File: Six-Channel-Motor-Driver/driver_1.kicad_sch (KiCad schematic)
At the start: 9 parts, among them J2 Screw_Terminal_01x02, Q1 Q_NMOS_GDS, Q2 Q_NMOS_GDS, Q3 Q_NMOS_GDS, Q4 Q_NMOS_GDS

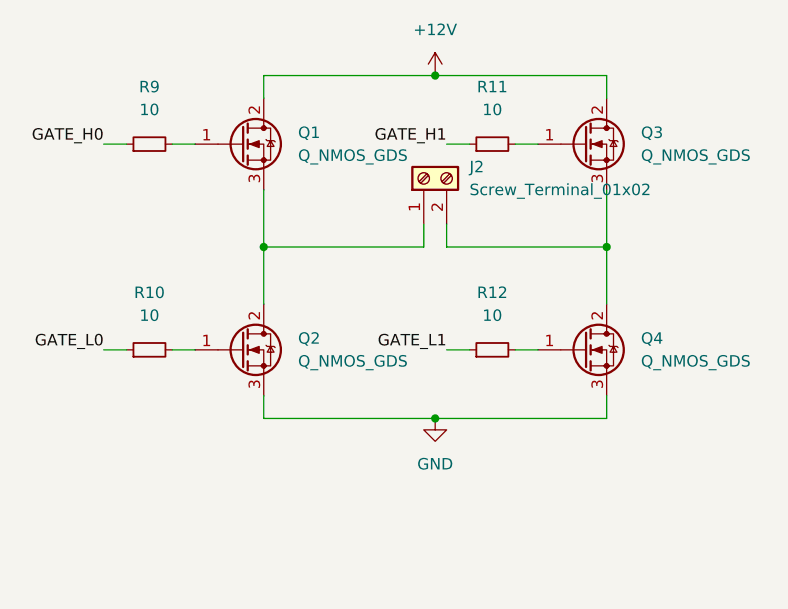
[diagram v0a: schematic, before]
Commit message: Added start of driver blocks
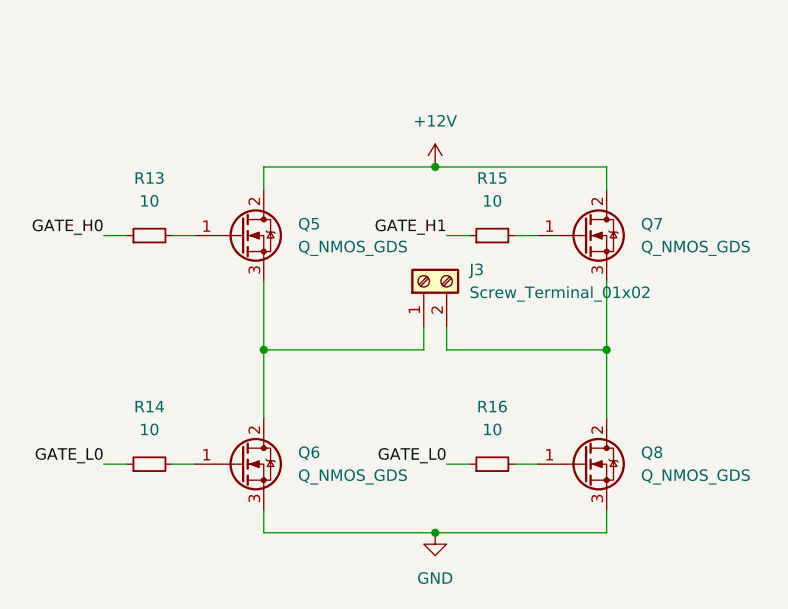
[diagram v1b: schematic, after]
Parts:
- removed J2: Screw_Terminal_01x02, Connector_Wire:SolderWire-2.5sqmm_1x02_P8.8mm_D2.4mm_OD4.4mm, symbol Connector:Screw_Terminal_01x02
- removed Q1, Q2, Q3, Q4: Q_NMOS_GDS, Package_TO_SOT_SMD:SOT-23, symbol Device:Q_NMOS_GDS
- removed R10, R11, R12, R9: 10, Resistor_SMD:R_0603_1608Metric, symbol Device:R_Small
- added J3: Screw_Terminal_01x02, Connector_Wire:SolderWire-2.5sqmm_1x02_P8.8mm_D2.4mm_OD4.4mm, symbol Connector:Screw_Terminal_01x02
- added Q5, Q6, Q7, Q8: Q_NMOS_GDS, Package_TO_SOT_SMD:SOT-23, symbol Device:Q_NMOS_GDS
- added R13, R14, R15, R16: 10, Resistor_SMD:R_0603_1608Metric, symbol Device:R_Small
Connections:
- net +12V: now also Q5.2 (D), Q7.2 (D)
- net GATE_H0: now also R13.1
- net GATE_H1: now also R15.1
- net GATE_L0: now also R14.1, R16.1
- net GND: now also Q6.3 (S), Q8.3 (S)
- new net: Q6.1 (G), R14.2
- new net: Q7.1 (G), R15.2
- new net: J3.2 (Pin_2), Q7.3 (S), Q8.2 (D)
- new net: Q8.1 (G), R16.2
- new net: J3.1 (Pin_1), Q5.3 (S), Q6.2 (D)
- new net: Q5.1 (G), R13.2
